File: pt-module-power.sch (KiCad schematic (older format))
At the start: 30 parts

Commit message: Connected EVERYTHING. Ran ERC. There are still some power errors.
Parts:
- gave numbers to parts that had none: 30
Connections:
- net +3V3: now also C10.1, C9.1
- net VCC: now also C6.1
- net at L3.1, U3.6 (SW): now also C8.2, D7.1 (K)

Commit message: fix power scheme
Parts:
- removed C1: 100nF, symbol C_Small
- removed C2: 22uF 6.3V, symbol C
- removed D1: 10V, Diodes_SMD:D_SOD-323, symbol D_Zener_Small
- removed D2: STTH102A, Diodes_SMD:D_SMA, symbol D
- removed D3: DB2J317, Diodes_SMD:D_SOD-323, symbol D_Schottky
- removed L1: 15uH, Inductors_SMD:L_Taiyo-Yuden_NR-40xx_HandSoldering, symbol L
- removed R1: 10k, symbol R
- removed R2: 31.6k, symbol R
- removed U1: MCP16331, TO_SOT_Packages_SMD:SOT-23-6, symbol MCP16331
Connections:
- no-connect marks 2 -> 1
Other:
- note added: "Switching Regulator\n+4.5..50V in, +3.3V/500mA out"
- note removed: "Suggested regulator\n+6..50V in, +3.3V/500mA out"
- note removed: "Switching Regulator\n+15V in, +3.3V/500mA out"
- moved on the sheet: C10, C6, C7, C8, C9, D7, D8, L3, R5, R6, U3

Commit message: Re-annotation
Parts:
- renumbered C6 to C1, C7 to C2, C8 to C4, C4 to C5, C5 to C6, C9 to C7, C10 to C8, D4 to D1, D7 to D2, D8 to D3, D5 to D4, D6 to D5, L2 to L1, L3 to L2, R5 to R1, R6 to R2, U2 to U1, U3 to U2
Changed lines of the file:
@@
 $EndDescr
 $Comp
-L MCP16331 U3
+L MCP16331 U2
 U 1 1 598C3113
 P 5250 4500
-F 0 "U3" H 5250 4525 60  0000 C CNN
+F 0 "U2" H 5250 4525 60  0000 C CNN
 F 1 "MCP16331" H 5250 4900 60  0000 C CNN
 F 2 "TO_SOT_Packages_SMD:SOT-23-6" H 5250 4350 60  0001 C CNN
@@
 $EndComp
 $Comp
-L VCC #PWR025
+L VCC #PWR17
 U 1 1 598C3307
 P 3600 4400
-F 0 "#PWR025" H 3600 4250 50  0001 C CNN
+F 0 "#PWR17" H 3600 4250 50  0001 C CNN
 F 1 "VCC" H 3600 4550 50  0000 C CNN
 F 2 "" H 3600 4400 50  0001 C CNN
@@
 NoConn ~ 4700 4600
 $Comp
-L C C7
+L C C2
 U 1 1 598C33D3
 P 4050 4550
-F 0 "C7" H 4075 4650 50  0000 L CNN
+F 0 "C2" H 4075 4650 50  0000 L CNN
 F 1 "10 µF" H 4075 4450 50  0000 L CNN
 F 2 "" H 4088 4400 50  0001 C CNN
@@
 $EndComp
 $Comp
-L GND #PWR026
+L GND #PWR20
 U 1 1 598C36A8
 P 4050 4700
-F 0 "#PWR026" H 4050 4450 50  0001 C CNN
+F 0 "#PWR20" H 4050 4450 50  0001 C CNN
 F 1 "GND" H 4050 4550 50  0000 C CNN
 F 2 "" H 4050 4700 50  0001 C CNN
@@
 $EndComp
 $Comp
-L GND #PWR027
+L GND #PWR21
 U 1 1 598C3B7E
 P 5250 5050
-F 0 "#PWR027" H 5250 4800 50  0001 C CNN
+F 0 "#PWR21" H 5250 4800 50  0001 C CNN
 F 1 "GND" H 5250 4900 50  0000 C CNN
 F 2 "" H 5250 5050 50  0001 C CNN
@@
 $EndComp
 $Comp
-L GND #PWR028
+L GND #PWR24
 U 1 1 598C3C64
 P 6550 5500
-F 0 "#PWR028" H 6550 5250 50  0001 C CNN
+F 0 "#PWR24" H 6550 5250 50  0001 C CNN
 F 1 "GND" H 6550 5350 50  0000 C CNN
 F 2 "" H 6550 5500 50  0001 C CNN
@@
 $EndComp
 $Comp
-L R R6
+L R R2
 U 1 1 598C3CEB
 P 6550 5350
-F 0 "R6" V 6630 5350 50  0000 C CNN
+F 0 "R2" V 6630 5350 50  0000 C CNN
 F 1 "10k" V 6550 5350 50  0000 C CNN
 F 2 "" V 6480 5350 50  0001 C CNN
@@
 $EndComp
 $Comp
-L R R5
+L R R1
 U 1 1 598C4622
 P 6550 5050
-F 0 "R5" V 6630 5050 50  0000 C CNN
+F 0 "R1" V 6630 5050 50  0000 C CNN
 F 1 "31k" V 6550 5050 50  0000 C CNN
 F 2 "" V 6480 5050 50  0001 C CNN
@@
 $EndComp
 $Comp
-L D_Schottky D7
+L D_Schottky D2
 U 1 1 598C4B08
 P 6250 4650
-F 0 "D7" H 6250 4750 50  0000 C CNN
+F 0 "D2" H 6250 4750 50  0000 C CNN
 F 1 "D_Schottky" H 6250 4550 50  0000 C CNN
 F 2 "" H 6250 4650 50  0001 C CNN
@@
 $EndComp
 $Comp
-L GND #PWR029
+L GND #PWR23
 U 1 1 598C5043
 P 6250 4800
-F 0 "#PWR029" H 6250 4550 50  0001 C CNN
+F 0 "#PWR23" H 6250 4550 50  0001 C CNN
 F 1 "GND" H 6250 4650 50  0000 C CNN
 F 2 "" H 6250 4800 50  0001 C CNN
@@
 $EndComp
 $Comp
-L L L3
+L L L2
 U 1 1 598C5640
 P 6550 4650
-F 0 "L3" V 6500 4650 50  0000 C CNN
+F 0 "L2" V 6500 4650 50  0000 C CNN
 F 1 "15µH" V 6625 4650 50  0000 C CNN
 F 2 "" H 6550 4650 50  0001 C CNN
@@
 $EndComp
 $Comp
-L C C8
+L C C4
 U 1 1 598C7BBA
 P 5850 4350
-F 0 "C8" H 5875 4450 50  0000 L CNN
+F 0 "C4" H 5875 4450 50  0000 L CNN
 F 1 "100nF" H 5875 4250 50  0000 L CNN
 F 2 "" H 5888 4200 50  0001 C CNN
@@
 $EndComp
 $Comp
-L D D8
+L D D3
 U 1 1 598C7D46
 P 6300 4200
-F 0 "D8" H 6300 4300 50  0000 C CNN
+F 0 "D3" H 6300 4300 50  0000 C CNN
 F 1 "D" H 6300 4100 50  0000 C CNN
 F 2 "" H 6300 4200 50  0001 C CNN
@@
 $EndComp
 $Comp
-L +3.3V #PWR030
+L +3.3V #PWR27
 U 1 1 598C94DC
 P 7500 4600
-F 0 "#PWR030" H 7500 4450 50  0001 C CNN
+F 0 "#PWR27" H 7500 4450 50  0001 C CNN
 F 1 "+3.3V" H 7500 4740 50  0000 C CNN
 F 2 "" H 7500 4600 50  0001 C CNN
@@
 $EndComp
 $Comp
-L PWR_FLAG #FLG031
+L PWR_FLAG #FLG2
 U 1 1 598C9528
 P 7750 4850
-F 0 "#FLG031" H 7750 4925 50  0001 C CNN
+F 0 "#FLG2" H 7750 4925 50  0001 C CNN
 F 1 "PWR_FLAG" H 7750 5000 50  0000 C CNN
 F 2 "" H 7750 4850 50  0001 C CNN
@@
 $EndComp
 $Comp
-L GND #PWR032
+L GND #PWR25
 U 1 1 598CA371
 P 6900 5150
-F 0 "#PWR032" H 6900 4900 50  0001 C CNN
+F 0 "#PWR25" H 6900 4900 50  0001 C CNN
 F 1 "GND" H 6900 5000 50  0000 C CNN
 F 2 "" H 6900 5150 50  0001 C CNN
@@
 Switching Regulator\n+4.5..50V in, +3.3V/500mA out
 $Comp
-L C C9
+L C C7
 U 1 1 598C8ED1
 P 6900 5000
-F 0 "C9" H 6925 5100 50  0000 L CNN
+F 0 "C7" H 6925 5100 50  0000 L CNN
 F 1 "10 µF" H 6925 4900 50  0000 L CNN
 F 2 "" H 6938 4850 50  0001 C CNN
@@
 $EndComp
 $Comp
-L C C6
+L C C1
 U 1 1 598CEAC9
 P 3700 4550
-F 0 "C6" H 3725 4650 50  0000 L CNN
+F 0 "C1" H 3725 4650 50  0000 L CNN
 F 1 "10 µF" H 3725 4450 50  0000 L CNN
 F 2 "" H 3738 4400 50  0001 C CNN
@@
 $EndComp
 $Comp
-L GND #PWR033
+L GND #PWR18
 U 1 1 598CEACF
 P 3700 4700
-F 0 "#PWR033" H 3700 4450 50  0001 C CNN
+F 0 "#PWR18" H 3700 4450 50  0001 C CNN
 F 1 "GND" H 3700 4550 50  0000 C CNN
 F 2 "" H 3700 4700 50  0001 C CNN
@@
 $EndComp
 $Comp
-L GND #PWR034
+L GND #PWR26
 U 1 1 598CEF8A
 P 7350 5150
-F 0 "#PWR034" H 7350 4900 50  0001 C CNN
+F 0 "#PWR26" H 7350 4900 50  0001 C CNN
 F 1 "GND" H 7350 5000 50  0000 C CNN
 F 2 "" H 7350 5150 50  0001 C CNN
@@
 $EndComp
 $Comp
-L C C10
+L C C8
 U 1 1 598CEF90
 P 7350 5000
-F 0 "C10" H 7375 5100 50  0000 L CNN
+F 0 "C8" H 7375 5100 50  0000 L CNN
 F 1 "10 µF" H 7375 4900 50  0000 L CNN
 F 2 "" H 7388 4850 50  0001 C CNN
@@
 External_VCC
 $Comp
-L PWR_FLAG #FLG022
+L PWR_FLAG #FLG1
 U 1 1 597BEB38
 P 7725 2225
-F 0 "#FLG022" H 7725 2300 50  0001 C CNN
+F 0 "#FLG1" H 7725 2300 50  0001 C CNN
 F 1 "PWR_FLAG" H 7725 2375 50  0000 C CNN
 F 2 "" H 7725 2225 50  0001 C CNN
@@
 $EndComp
 $Comp
-L C C5
+L C C6
 U 1 1 597A079A
 P 6650 2525
-F 0 "C5" V 6500 2475 50  0000 L CNN
+F 0 "C6" V 6500 2475 50  0000 L CNN
 F 1 "22uF 25V" V 6775 2350 50  0000 L CNN
 F 2 "" H 6688 2375 50  0001 C CNN
@@
 $EndComp
 $Comp
-L GND #PWR018
+L GND #PWR22
 U 1 1 597A23E8
 P 5675 3100
-F 0 "#PWR018" H 5675 2850 50  0001 C CNN
+F 0 "#PWR22" H 5675 2850 50  0001 C CNN
 F 1 "GND" H 5675 2950 50  0000 C CNN
 F 2 "" H 5675 3100 50  0001 C CNN
@@
 $EndComp
 $Comp
-L D_Zener_Small D6
+L D_Zener_Small D5
 U 1 1 597A1DBE
 P 6700 1975
-F 0 "D6" H 6700 1885 50  0000 C CNN
+F 0 "D5" H 6700 1885 50  0000 C CNN
 F 1 "10V" H 6700 2085 50  0000 C CNN
 F 2 "Diodes_SMD:D_SOD-323" V 6700 1975 50  0001 C CNN
@@
 $EndComp
 $Comp
-L C_Small C4
+L C_Small C5
 U 1 1 597A00D9
 P 5950 2125
-F 0 "C4" V 5825 2075 50  0000 L CNN
+F 0 "C5" V 5825 2075 50  0000 L CNN
 F 1 "100nF" V 6050 2000 50  0000 L CNN
 F 2 "" H 5950 2125 50  0001 C CNN
@@
 $EndComp
 $Comp
-L D D5
+L D D4
 U 1 1 5979FF78
 P 6325 1975
-F 0 "D5" H 6325 2075 50  0000 C CNN
+F 0 "D4" H 6325 2075 50  0000 C CNN
 F 1 "STTH102A" H 6325 1875 50  0000 C CNN
 F 2 "Diodes_SMD:D_SMA" H 6325 1975 50  0001 C CNN
@@
 $EndComp
 $Comp
-L D_Schottky D4
+L D_Schottky D1
 U 1 1 5979FBA7
 P 5950 2500
-F 0 "D4" H 5950 2400 50  0000 C CNN
+F 0 "D1" H 5950 2400 50  0000 C CNN
 F 1 "B1100/B" H 5950 2600 50  0000 C CNN
 F 2 "Diodes_SMD:D_SMB" H 5950 2500 50  0001 C CNN
@@
 $EndComp
 $Comp
-L L L2
+L L L1
 U 1 1 5979FADF
 P 6300 2275
-F 0 "L2" V 6250 2275 50  0000 C CNN
+F 0 "L1" V 6250 2275 50  0000 C CNN
 F 1 "68uH" V 6375 2275 50  0000 C CNN
 F 2 "Inductors_SMD:L_7.3x7.3_H4.5" H 6300 2275 50  0001 C CNN
@@
 PWREN
 $Comp
-L MCP16331 U2
+L MCP16331 U1
 U 1 1 597A1586
 P 5150 2275
-F 0 "U2" H 5150 2275 60  0000 C CNN
+F 0 "U1" H 5150 2275 60  0000 C CNN
 F 1 "MCP16331" H 5150 2675 60  0000 C CNN
 F 2 "TO_SOT_Packages_SMD:SOT-23-6" H 5150 2125 60  0001 C CNN
@@
 $EndComp
 $Comp
-L VDD #PWR017
+L VDD #PWR19
 U 1 1 597A11B1
 P 3800 2075
-F 0 "#PWR017" H 3800 1925 50  0001 C CNN
+F 0 "#PWR19" H 3800 1925 50  0001 C CNN
 F 1 "VDD" H 3800 2225 50  0000 C CNN
 F 2 "" H 3800 2075 50  0001 C CNN

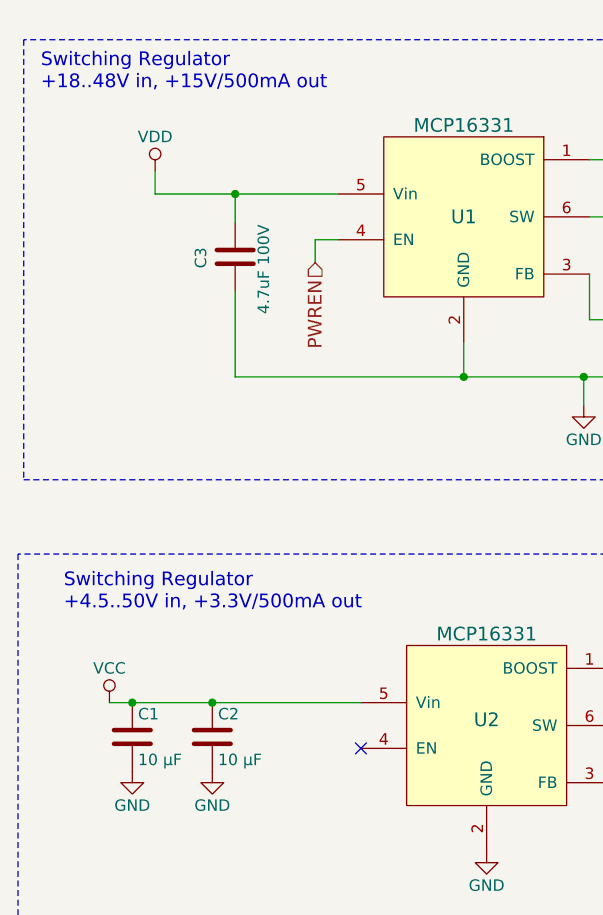
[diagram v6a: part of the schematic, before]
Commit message: Added power flags and ERC error count shrinked into 3.
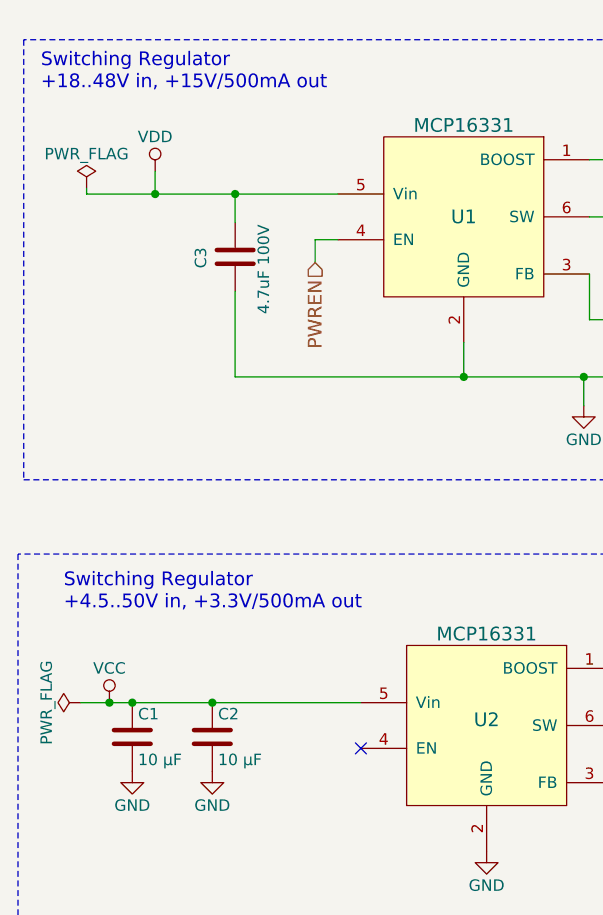
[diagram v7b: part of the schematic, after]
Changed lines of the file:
@@
 $EndComp
 $Comp
-L VCC #PWR17
+L VCC #PWR017
 U 1 1 598C3307
 P 3600 4400
-F 0 "#PWR17" H 3600 4250 50  0001 C CNN
+F 0 "#PWR017" H 3600 4250 50  0001 C CNN
 F 1 "VCC" H 3600 4550 50  0000 C CNN
 F 2 "" H 3600 4400 50  0001 C CNN
@@
 $EndComp
 $Comp
-L GND #PWR20
+L GND #PWR018
 U 1 1 598C36A8
 P 4050 4700
-F 0 "#PWR20" H 4050 4450 50  0001 C CNN
+F 0 "#PWR018" H 4050 4450 50  0001 C CNN
 F 1 "GND" H 4050 4550 50  0000 C CNN
 F 2 "" H 4050 4700 50  0001 C CNN
@@
 $EndComp
 $Comp
-L GND #PWR21
+L GND #PWR019
 U 1 1 598C3B7E
 P 5250 5050
-F 0 "#PWR21" H 5250 4800 50  0001 C CNN
+F 0 "#PWR019" H 5250 4800 50  0001 C CNN
 F 1 "GND" H 5250 4900 50  0000 C CNN
 F 2 "" H 5250 5050 50  0001 C CNN
@@
 $EndComp
 $Comp
-L GND #PWR24
+L GND #PWR020
 U 1 1 598C3C64
 P 6550 5500
-F 0 "#PWR24" H 6550 5250 50  0001 C CNN
+F 0 "#PWR020" H 6550 5250 50  0001 C CNN
 F 1 "GND" H 6550 5350 50  0000 C CNN
 F 2 "" H 6550 5500 50  0001 C CNN
@@
 $EndComp
 $Comp
-L GND #PWR23
+L GND #PWR021
 U 1 1 598C5043
 P 6250 4800
-F 0 "#PWR23" H 6250 4550 50  0001 C CNN
+F 0 "#PWR021" H 6250 4550 50  0001 C CNN
 F 1 "GND" H 6250 4650 50  0000 C CNN
 F 2 "" H 6250 4800 50  0001 C CNN
@@
 $EndComp
 $Comp
-L +3.3V #PWR27
+L +3.3V #PWR022
 U 1 1 598C94DC
 P 7500 4600
-F 0 "#PWR27" H 7500 4450 50  0001 C CNN
+F 0 "#PWR022" H 7500 4450 50  0001 C CNN
 F 1 "+3.3V" H 7500 4740 50  0000 C CNN
 F 2 "" H 7500 4600 50  0001 C CNN
@@
 $EndComp
 $Comp
-L PWR_FLAG #FLG2
+L PWR_FLAG #FLG023
 U 1 1 598C9528
 P 7750 4850
-F 0 "#FLG2" H 7750 4925 50  0001 C CNN
+F 0 "#FLG023" H 7750 4925 50  0001 C CNN
 F 1 "PWR_FLAG" H 7750 5000 50  0000 C CNN
 F 2 "" H 7750 4850 50  0001 C CNN
@@
 $EndComp
 $Comp
-L GND #PWR25
+L GND #PWR024
 U 1 1 598CA371
 P 6900 5150
-F 0 "#PWR25" H 6900 4900 50  0001 C CNN
+F 0 "#PWR024" H 6900 4900 50  0001 C CNN
 F 1 "GND" H 6900 5000 50  0000 C CNN
 F 2 "" H 6900 5150 50  0001 C CNN
@@
 $EndComp
 $Comp
-L GND #PWR18
+L GND #PWR025
 U 1 1 598CEACF
 P 3700 4700
-F 0 "#PWR18" H 3700 4450 50  0001 C CNN
+F 0 "#PWR025" H 3700 4450 50  0001 C CNN
 F 1 "GND" H 3700 4550 50  0000 C CNN
 F 2 "" H 3700 4700 50  0001 C CNN
@@
 $EndComp
 $Comp
-L GND #PWR26
+L GND #PWR026
 U 1 1 598CEF8A
 P 7350 5150
-F 0 "#PWR26" H 7350 4900 50  0001 C CNN
+F 0 "#PWR026" H 7350 4900 50  0001 C CNN
 F 1 "GND" H 7350 5000 50  0000 C CNN
 F 2 "" H 7350 5150 50  0001 C CNN
@@
 $EndComp
 Wire Wire Line
-	3600 4400 4700 4400
+	3475 4400 4700 4400
 Connection ~ 4050 4400
 Wire Wire Line
@@
 External_VCC
 $Comp
-L PWR_FLAG #FLG1
+L PWR_FLAG #FLG027
 U 1 1 597BEB38
 P 7725 2225
-F 0 "#FLG1" H 7725 2300 50  0001 C CNN
+F 0 "#FLG027" H 7725 2300 50  0001 C CNN
 F 1 "PWR_FLAG" H 7725 2375 50  0000 C CNN
 F 2 "" H 7725 2225 50  0001 C CNN
@@
 $EndComp
 $Comp
-L GND #PWR22
+L GND #PWR028
 U 1 1 597A23E8
 P 5675 3100
-F 0 "#PWR22" H 5675 2850 50  0001 C CNN
+F 0 "#PWR028" H 5675 2850 50  0001 C CNN
 F 1 "GND" H 5675 2950 50  0000 C CNN
 F 2 "" H 5675 3100 50  0001 C CNN
@@
 	4150 2175 4150 2300
 Wire Wire Line
-	3800 2175 4600 2175
+	3500 2175 4600 2175
 Wire Wire Line
 	3800 2075 3800 2175
@@
 $EndComp
 $Comp
-L VDD #PWR19
+L VDD #PWR029
 U 1 1 597A11B1
 P 3800 2075
-F 0 "#PWR19" H 3800 1925 50  0001 C CNN
+F 0 "#PWR029" H 3800 1925 50  0001 C CNN
 F 1 "VDD" H 3800 2225 50  0000 C CNN
 F 2 "" H 3800 2075 50  0001 C CNN
@@
 	1    0    0    -1
 $EndComp
+$Comp
+L PWR_FLAG #FLG030
+U 1 1 59948AC3
+P 3500 2150
+F 0 "#FLG030" H 3500 2225 50  0001 C CNN
+F 1 "PWR_FLAG" H 3500 2300 50  0000 C CNN
+F 2 "" H 3500 2150 50  0001 C CNN
+F 3 "" H 3500 2150 50  0001 C CNN
+	1    3500 2150
+	1    0    0    -1
+$EndComp
+Wire Wire Line
+	3500 2175 3500 2150
+Connection ~ 3800 2175
+$Comp
+L PWR_FLAG #FLG?
+U 1 1 59958159
+P 3475 4400
+F 0 "#FLG?" H 3475 4475 50  0001 C CNN
+F 1 "PWR_FLAG" H 3475 4550 50  0000 C CNN
+F 2 "" H 3475 4400 50  0001 C CNN
+F 3 "" H 3475 4400 50  0001 C CNN
+	1    3475 4400
+	0    -1   -1   0
+$EndComp
+Connection ~ 3600 4400
 $EndSCHEMATC
